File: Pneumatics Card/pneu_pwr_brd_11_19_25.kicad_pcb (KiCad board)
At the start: 4 copper layers, 65 x 65 mm, 79 parts, among them J1 2X1, J10 Conn_01x02, J11 Conn_01x02, J12 2X1, J13 2X1, J2 2X1, J3 2X1, J4 2X1, J5 2X1, J6 2X1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

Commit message: Change the M3 hole
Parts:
- C1: value 10nF -> 22nF
- C12: value 4.7u -> 0.47u
- H1, H2, H3, H4: footprint MountingHole:MountingHole_4.3mm_M4_ISO7380_Pad_TopBottom -> MountingHole:MountingHole_3.2mm_M3_DIN965
- R1: value 100k -> 1k
- R2: value 150k -> 4.7k
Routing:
- net 12V: vias 16 -> 20
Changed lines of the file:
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@@
 			)
 		)
-		(property "Value" "10nF"
+		(property "Value" "22nF"
 			(at 0 1.16 90)
 			(layer "F.Fab")
@@
 		)
 	)
-	(footprint "MountingHole:MountingHole_4.3mm_M4_ISO7380_Pad_TopBottom"
+	(footprint "MountingHole:MountingHole_3.2mm_M3_DIN965"
 		(layer "F.Cu")
 		(at 137.16 23.06)
-		(descr "Mounting Hole 4.3mm, M4, ISO7380")
-		(tags "mounting hole 4.3mm m4 iso7380")
+		(descr "Mounting Hole 3.2mm, no annular, M3, DIN965")
+		(tags "mounting hole 3.2mm no annular m3 din965")
 		(property "Reference" "H2"
-			(at 3.91 -3.34 0)
+			(at 0 -3.8 0)
 			(layer "F.SilkS")
 			(effects
@@
 		)
 		(property "Value" "MountingHole"
-			(at 0 4.8 0)
+			(at 0 3.8 0)
 			(layer "F.Fab")
 			(effects
@@
 		(fp_circle
 			(center 0 0)
-			(end 3.8 0)
+			(end 2.8 0)
 			(stroke
 				(width 0.15)
@@
 		(fp_circle
 			(center 0 0)
-			(end 4.05 0)
+			(end 3.05 0)
 			(stroke
 				(width 0.05)
@@
 			)
 		)
-		(pad "1" thru_hole circle
+		(pad "" np_thru_hole circle
 			(at 0 0)
-			(size 4.7 4.7)
-			(drill 4.3)
+			(size 3.2 3.2)
+			(drill 3.2)
 			(layers "*.Cu" "*.Mask")
-			(remove_unused_layers no)
-		)
-		(pad "1" connect circle
-			(at 0 0)
-			(size 7.6 7.6)
-			(layers "F.Cu" "F.Mask")
-		)
-		(pad "1" connect circle
-			(at 0 0)
-			(size 7.6 7.6)
-			(layers "B.Cu" "B.Mask")
 		)
 		(embedded_fonts no)
@@
 		)
 	)
-	(footprint "MountingHole:MountingHole_4.3mm_M4_ISO7380_Pad_TopBottom"
+	(footprint "MountingHole:MountingHole_3.2mm_M3_DIN965"
 		(layer "F.Cu")
 		(at 137.16 78.04)
-		(descr "Mounting Hole 4.3mm, M4, ISO7380")
-		(tags "mounting hole 4.3mm m4 iso7380")
+		(descr "Mounting Hole 3.2mm, no annular, M3, DIN965")
+		(tags "mounting hole 3.2mm no annular m3 din965")
 		(property "Reference" "H4"
-			(at 1.36 -4.72 0)
+			(at 0 -3.8 0)
 			(layer "F.SilkS")
 			(effects
@@
 		)
 		(property "Value" "MountingHole"
-			(at 0 4.8 0)
+			(at 0 3.8 0)
 			(layer "F.Fab")
 			(effects
@@
 		(fp_circle
 			(center 0 0)
-			(end 3.8 0)
+			(end 2.8 0)
 			(stroke
 				(width 0.15)
@@
 		(fp_circle
 			(center 0 0)
-			(end 4.05 0)
+			(end 3.05 0)
 			(stroke
 				(width 0.05)
@@
 			)
 		)
-		(pad "1" thru_hole circle
+		(pad "" np_thru_hole circle
 			(at 0 0)
-			(size 4.7 4.7)
-			(drill 4.3)
+			(size 3.2 3.2)
+			(drill 3.2)
 			(layers "*.Cu" "*.Mask")
-			(remove_unused_layers no)
-		)
-		(pad "1" connect circle
-			(at 0 0)
-			(size 7.6 7.6)
-			(layers "F.Cu" "F.Mask")
-		)
-		(pad "1" connect circle
-			(at 0 0)
-			(size 7.6 7.6)
-			(layers "B.Cu" "B.Mask")
 		)
 		(embedded_fonts no)
@@
 		)
 	)
-	(footprint "MountingHole:MountingHole_4.3mm_M4_ISO7380_Pad_TopBottom"
+	(footprint "MountingHole:MountingHole_3.2mm_M3_DIN965"
 		(layer "F.Cu")
 		(at 84.14 23.06)
-		(descr "Mounting Hole 4.3mm, M4, ISO7380")
-		(tags "mounting hole 4.3mm m4 iso7380")
+		(descr "Mounting Hole 3.2mm, no annular, M3, DIN965")
+		(tags "mounting hole 3.2mm no annular m3 din965")
 		(property "Reference" "H1"
-			(at 5.02 -2.67 0)
+			(at 0 -3.8 0)
 			(layer "F.SilkS")
 			(effects
@@
 		)
 		(property "Value" "MountingHole"
-			(at 0 4.8 0)
+			(at 0 3.8 0)
 			(layer "F.Fab")
 			(effects
@@
 		(fp_circle
 			(center 0 0)
-			(end 3.8 0)
+			(end 2.8 0)
 			(stroke
 				(width 0.15)
@@
 		(fp_circle
 			(center 0 0)
-			(end 4.05 0)
+			(end 3.05 0)
 			(stroke
 				(width 0.05)
@@
 			)
 		)
-		(pad "1" thru_hole circle
+		(pad "" np_thru_hole circle
 			(at 0 0)
-			(size 4.7 4.7)
-			(drill 4.3)
+			(size 3.2 3.2)
+			(drill 3.2)
 			(layers "*.Cu" "*.Mask")
-			(remove_unused_layers no)
-		)
-		(pad "1" connect circle
-			(at 0 0)
-			(size 7.6 7.6)
-			(layers "F.Cu" "F.Mask")
-		)
-		(pad "1" connect circle
-			(at 0 0)
-			(size 7.6 7.6)
-			(layers "B.Cu" "B.Mask")
 		)
 		(embedded_fonts no)
@@
 			)
 		)
-		(property "Value" "150k"
+		(property "Value" "4.7k"
 			(at 0 1.17 90)
 			(layer "F.Fab")
@@
 		)
 	)
-	(footprint "MountingHole:MountingHole_4.3mm_M4_ISO7380_Pad_TopBottom"
+	(footprint "MountingHole:MountingHole_3.2mm_M3_DIN965"
 		(layer "F.Cu")
 		(at 84.14 78.04)
-		(descr "Mounting Hole 4.3mm, M4, ISO7380")
-		(tags "mounting hole 4.3mm m4 iso7380")
+		(descr "Mounting Hole 3.2mm, no annular, M3, DIN965")
+		(tags "mounting hole 3.2mm no annular m3 din965")
 		(property "Reference" "H3"
-			(at 0 -4.8 0)
+			(at 0 -3.8 0)
 			(layer "F.SilkS")
 			(effects
@@
 		)
 		(property "Value" "MountingHole"
-			(at 0 4.8 0)
+			(at 0 3.8 0)
 			(layer "F.Fab")
 			(effects
@@
 		(fp_circle
 			(center 0 0)
-			(end 3.8 0)
+			(end 2.8 0)
 			(stroke
 				(width 0.15)
@@
 		(fp_circle
 			(center 0 0)
-			(end 4.05 0)
+			(end 3.05 0)
 			(stroke
 				(width 0.05)
@@
 			)
 		)
-		(pad "1" thru_hole circle
+		(pad "" np_thru_hole circle
 			(at 0 0)
-			(size 4.7 4.7)
-			(drill 4.3)
+			(size 3.2 3.2)
+			(drill 3.2)
 			(layers "*.Cu" "*.Mask")
-			(remove_unused_layers no)
-		)
-		(pad "1" connect circle
-			(at 0 0)
-			(size 7.6 7.6)
-			(layers "F.Cu" "F.Mask")
-		)
-		(pad "1" connect circle
-			(at 0 0)
-			(size 7.6 7.6)
-			(layers "B.Cu" "B.Mask")
 		)
 		(embedded_fonts no)
@@
 			)
 		)
-		(property "Value" "100k"
+		(property "Value" "1k"
 			(at 0 1.17 90)
 			(layer "F.Fab")
@@
 			)
 		)
-		(property "Value" "4.7u"
+		(property "Value" "0.47u"
 			(at 0 1.16 90)
 			(layer "F.Fab")
@@
 	)
 	(via
+		(at 89.58 70.41)
+		(size 0.8)
+		(drill 0.4)
+		(layers "F.Cu" "B.Cu")
+		(free yes)
+		(net 13)
+	)
+	(via
 		(at 92.59 71.38)
 		(size 0.8)
@@
 	)
 	(via
+		(at 91.58 70.41)
+		(size 0.8)
+		(drill 0.4)
+		(layers "F.Cu" "B.Cu")
+		(free yes)
+		(net 13)
+	)
+	(via
 		(at 90.6 73.36)
 		(size 0.8)
@@
 	)
 	(via
+		(at 90.58 70.41)
+		(size 0.8)
+		(drill 0.4)
+		(layers "F.Cu" "B.Cu")
+		(free yes)
+		(net 13)
+	)
+	(via
 		(at 89.4025 42.6925)
 		(size 0.8)
@@
 		(size 0.8)
 		(drill 0.4)
+		(layers "F.Cu" "B.Cu")
+		(free yes)
+		(net 13)
+	)
+	(via
+		(at 92.57 70.43)
+		(size 0.8)
+		(drill 0.4)

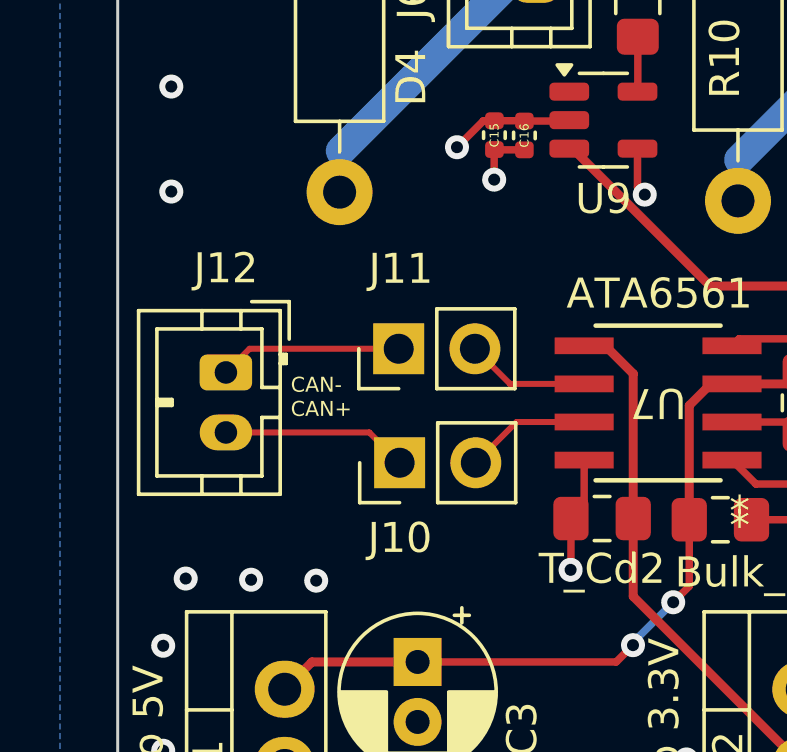
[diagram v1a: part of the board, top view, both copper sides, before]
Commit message: Corrected CANBUS routing Length.
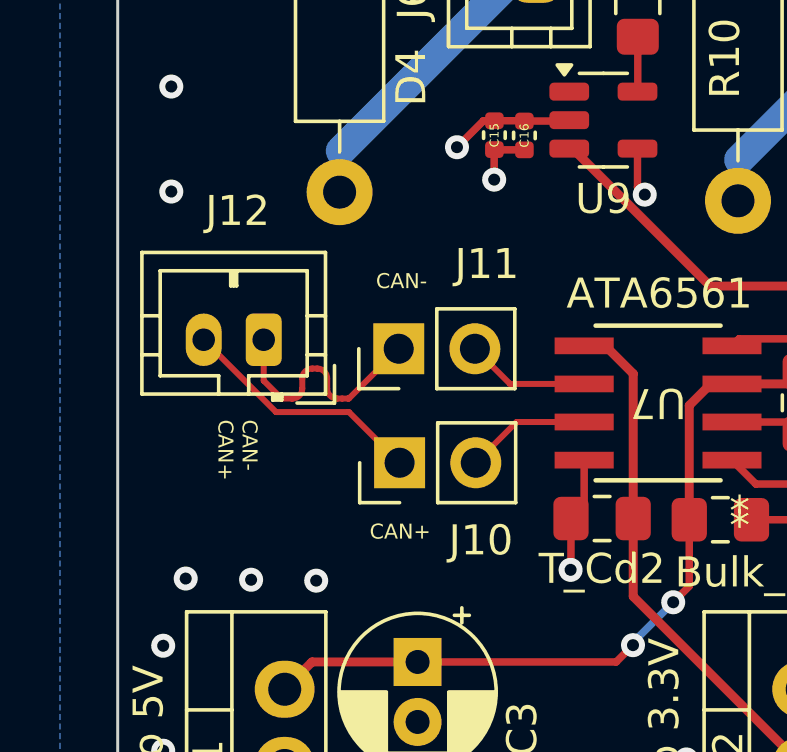
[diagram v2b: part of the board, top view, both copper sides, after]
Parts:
- moved J12 1.67 mm to (83.0, 49.1), turned to 180 degrees
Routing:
- net CAN-: track 10.2 -> 12.3 mm
- net CAN+: track 10.4 -> 12.4 mm
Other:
- board text added: "CAN+"
- board text added: "CAN-"

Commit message: Changed resistor values
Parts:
- C1: value 22nF -> 2.2uF
- R1: value 1k -> 47k
- R2: value 4.7k -> 10k
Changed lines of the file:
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@@
 			(psa4output no)
 			(plot_black_and_white yes)
-			(plotinvisibletext no)
 			(sketchpadsonfab no)
 			(plotpadnumbers no)
@@
 			)
 		)
-		(property "Datasheet" ""
+		(property "Datasheet" "~"
 			(at 0 0 90)
 			(unlocked yes)
@@
 			)
 		)
-		(property "Datasheet" ""
+		(property "Datasheet" "~"
 			(at 0 0 180)
 			(unlocked yes)
@@
 			)
 		)
-		(property "Datasheet" ""
+		(property "Datasheet" "~"
 			(at 0 0 90)
 			(unlocked yes)
@@
 			)
 		)
-		(property "Datasheet" ""
+		(property "Datasheet" "~"
 			(at 0 0 90)
 			(unlocked yes)
@@
 			)
 		)
-		(property "Datasheet" ""
+		(property "Datasheet" "~"
 			(at 0 0 90)
 			(layer "F.Fab")
@@
 			)
 		)
-		(property "Datasheet" ""
+		(property "Datasheet" "~"
 			(at 0 0 90)
 			(unlocked yes)
@@
 			)
 		)
-		(property "Datasheet" ""
+		(property "Datasheet" "~"
 			(at 0 0 90)
 			(layer "F.Fab")
@@
 			)
 		)
-		(property "Datasheet" ""
+		(property "Datasheet" "~"
 			(at 0 0 90)
 			(unlocked yes)
@@
 			)
 		)
-		(property "Value" "22nF"
+		(property "Value" "2.2uF"
 			(at 0 1.16 90)
 			(layer "F.Fab")
@@
 			)
 		)
-		(property "Datasheet" ""
+		(property "Datasheet" "~"
 			(at 0 0 90)
 			(unlocked yes)
@@
 			)
 		)
-		(property "Datasheet" ""
+		(property "Datasheet" "~"
 			(at 0 0 0)
 			(unlocked yes)
@@
 			)
 		)
-		(property "Datasheet" ""
+		(property "Datasheet" "~"
 			(at 0 0 0)
 			(unlocked yes)
@@
 			)
 		)
-		(property "Datasheet" ""
+		(property "Datasheet" "~"
 			(at 0 0 0)
 			(unlocked yes)
@@
 			)
 		)
-		(property "Datasheet" ""
+		(property "Datasheet" "~"
 			(at 0 0 90)
 			(layer "F.Fab")
@@
 			)
 		)
-		(property "Datasheet" ""
+		(property "Datasheet" "~"
 			(at 0 0 180)
 			(unlocked yes)
@@
 			)
 		)
-		(property "Datasheet" ""
+		(property "Datasheet" "~"
 			(at 0 0 0)
 			(layer "F.Fab")
@@
 			)
 		)
-		(property "Datasheet" ""
+		(property "Datasheet" "~"
 			(at 0 0 0)
 			(unlocked yes)
@@
 			)
 		)
-		(property "Datasheet" ""
+		(property "Datasheet" "~"
 			(at 0 0 0)
 			(unlocked yes)
@@
 			)
 		)
-		(property "Datasheet" ""
+		(property "Datasheet" "~"
 			(at 0 0 0)
 			(unlocked yes)
@@
 			)
 		)
-		(property "Datasheet" ""
+		(property "Datasheet" "~"
 			(at 0 0 0)
 			(unlocked yes)
@@
 			)
 		)
-		(property "Datasheet" ""
+		(property "Datasheet" "~"
 			(at 0 0 270)
 			(unlocked yes)
@@
 			)
 		)
-		(property "Datasheet" ""
+		(property "Datasheet" "~"
 			(at 0 0 0)
 			(unlocked yes)
@@
 			)
 		)
-		(property "Datasheet" ""
+		(property "Datasheet" "~"
 			(at 0 0 0)
 			(unlocked yes)
@@
 			)
 		)
-		(property "Datasheet" ""
+		(property "Datasheet" "~"
 			(at 0 0 90)
 			(unlocked yes)
@@
 			)
 		)
-		(property "Datasheet" ""
+		(property "Datasheet" "~"
 			(at 0 0 0)
 			(unlocked yes)
@@
 			)
 		)
-		(property "Datasheet" ""
+		(property "Datasheet" "~"
 			(at 0 0 0)
 			(layer "F.Fab")
@@
 			)
 		)
-		(property "Datasheet" ""
+		(property "Datasheet" "~"
 			(at 0 0 270)
 			(unlocked yes)
@@
 			)
 		)
-		(property "Datasheet" ""
+		(property "Datasheet" "~"
 			(at 0 0 270)
 			(unlocked yes)
@@
 			)
 		)
-		(property "Datasheet" ""
+		(property "Datasheet" "~"
 			(at 0 0 270)
 			(unlocked yes)
@@
 			)
 		)
-		(property "Datasheet" ""
+		(property "Datasheet" "~"
 			(at 0 0 180)
 			(unlocked yes)
@@
 			)
 		)
-		(property "Datasheet" ""
+		(property "Datasheet" "~"
 			(at 0 0 90)
 			(layer "F.Fab")
@@
 			)
 		)
-		(property "Datasheet" ""
+		(property "Datasheet" "~"
 			(at 0 0 90)
 			(unlocked yes)
@@
 			)
 		)
-		(property "Datasheet" ""
+		(property "Datasheet" "~"
 			(at 0 0 180)
 			(unlocked yes)
@@
 			)
 		)
-		(property "Value" "4.7k"
+		(property "Value" "10k"
 			(at 0 1.17 90)
 			(layer "F.Fab")
@@
 			)
 		)
-		(property "Datasheet" ""
+		(property "Datasheet" "~"
 			(at 0 0 90)
 			(layer "F.Fab")
@@
 			)
 		)
-		(property "Datasheet" ""
+		(property "Datasheet" "~"
 			(at 0 0 180)
 			(unlocked yes)
@@
 			)
 		)
-		(property "Datasheet" ""
+		(property "Datasheet" "~"
 			(at 0 0 90)
 			(unlocked yes)
@@
 			)
 		)
-		(property "Datasheet" ""
+		(property "Datasheet" "~"
 			(at 0 0 270)
 			(unlocked yes)
@@
 			)
 		)
-		(property "Datasheet" ""
+		(property "Datasheet" "~"
 			(at 0 0 90)
 			(layer "F.Fab")
@@
 			)
 		)
-		(property "Datasheet" ""
+		(property "Datasheet" "~"
 			(at 0 0 0)
 			(unlocked yes)
@@
 			)
 		)
-		(property "Value" "1k"
+		(property "Value" "47k"
 			(at 0 1.17 90)
 			(layer "F.Fab")
@@
 			)
 		)
-		(property "Datasheet" ""
+		(property "Datasheet" "~"
 			(at 0 0 90)
 			(layer "F.Fab")
@@
 			)
 		)
-		(property "Datasheet" ""
+		(property "Datasheet" "~"
 			(at 0 0 90)
 			(unlocked yes)
@@
 			)
 		)
-		(property "Datasheet" ""
+		(property "Datasheet" "~"
 			(at 0 0 90)
 			(unlocked yes)
@@
 			)
 		)
-		(property "Datasheet" ""
+		(property "Datasheet" "~"
 			(at 0 0 0)
 			(layer "F.Fab")
@@
 			)
 		)
-		(property "Datasheet" ""
+		(property "Datasheet" "~"
 			(at 0 0 90)
 			(unlocked yes)
@@
 			)
 		)
-		(property "Datasheet" ""
+		(property "Datasheet" "~"
 			(at 0 0 90)
 			(unlocked yes)

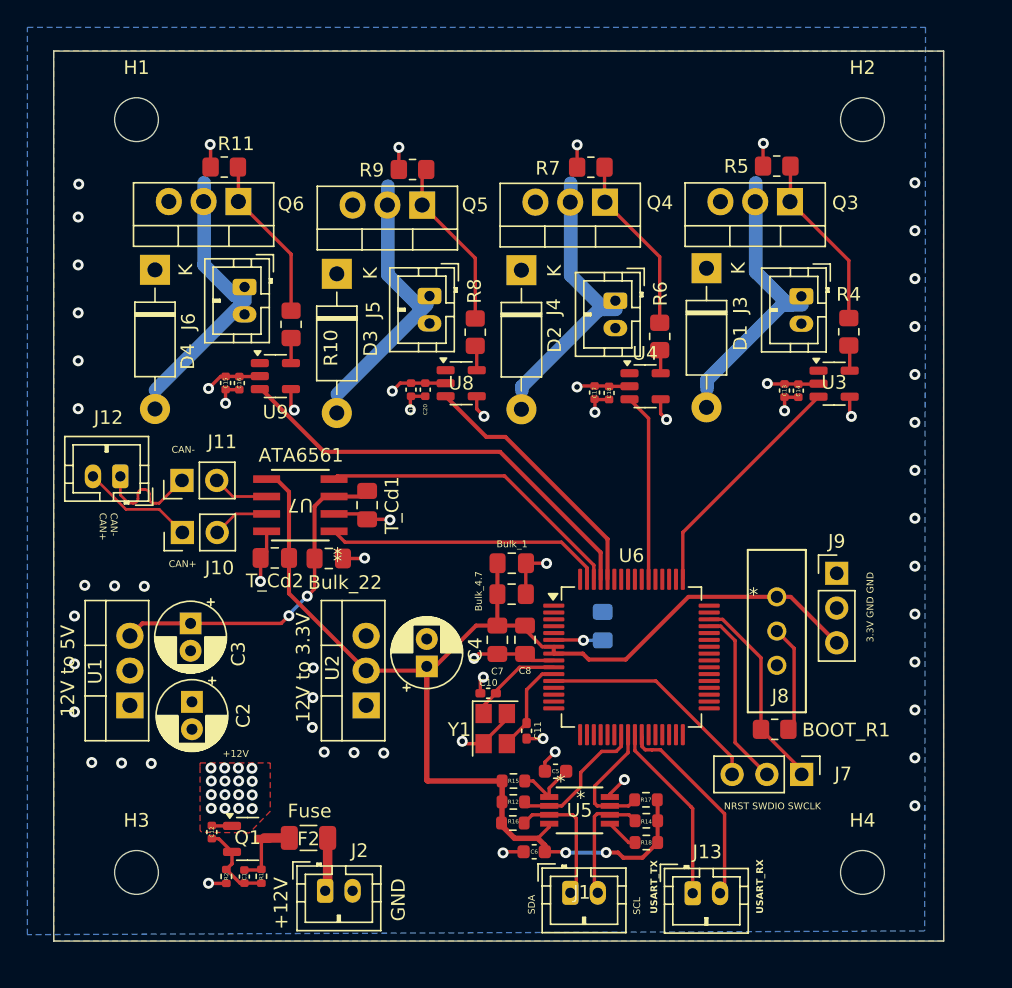
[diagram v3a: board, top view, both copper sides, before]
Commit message: fixed the traces, added test point, fixed some silkscreen
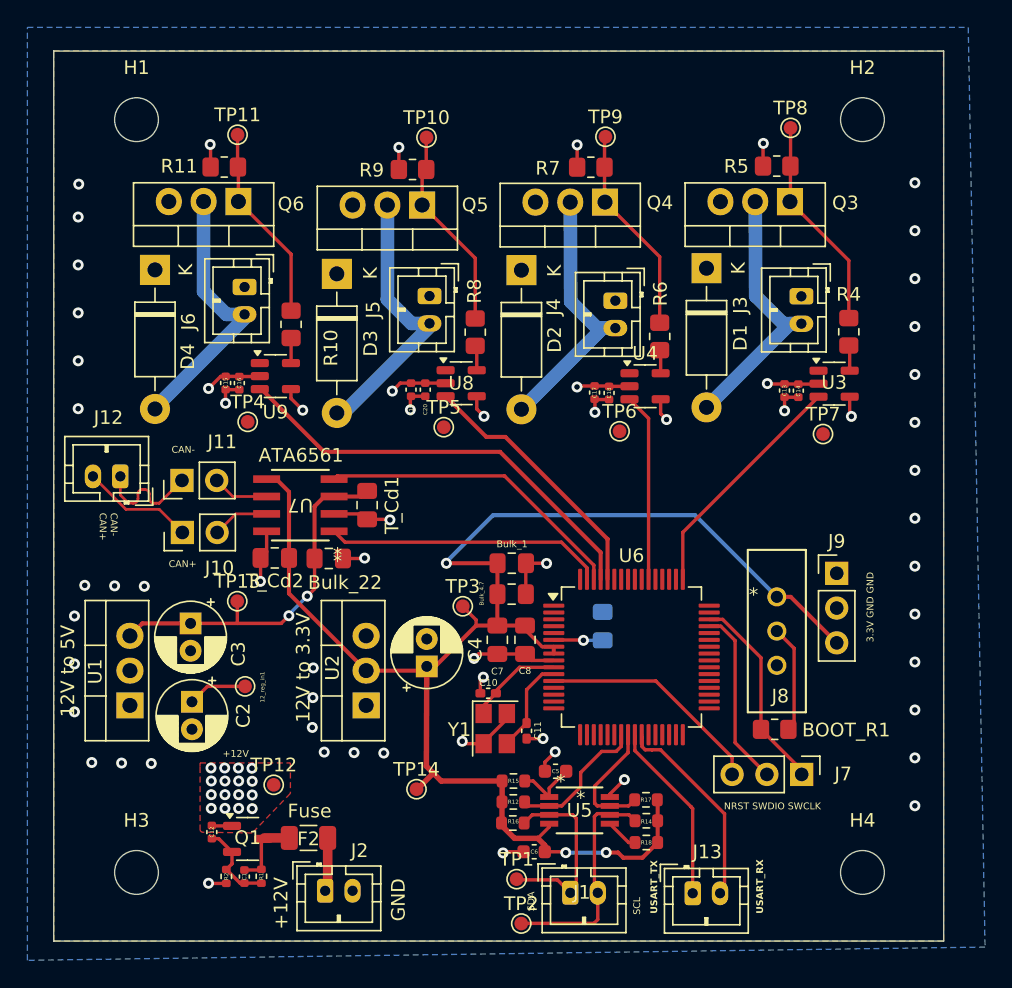
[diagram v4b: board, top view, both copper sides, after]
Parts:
- added 12_reg_in1: 12_reg_in, TestPoint:TestPoint_Pad_D1.0mm, F.Cu at (92.1, 64.5)
- added TP1: SDA_ext, TestPoint:TestPoint_Pad_D1.0mm, F.Cu at (111.9, 78.5)
- added TP10: S3_out, TestPoint:TestPoint_Pad_D1.0mm, F.Cu at (105.3, 24.4)
- added TP11: S4_out, TestPoint:TestPoint_Pad_D1.0mm, F.Cu at (91.5, 24.2)
- added TP12: 12V_PWR, TestPoint:TestPoint_Pad_D1.0mm, F.Cu at (94.2, 71.6)
- added TP13: 5_reg_out, TestPoint:TestPoint_Pad_D1.0mm, F.Cu at (91.5, 58.2)
- added TP14: 3.3_reg_out, TestPoint:TestPoint_Pad_D1.0mm, F.Cu at (104.6, 72.0)
- added TP2: SCL_ext, TestPoint:TestPoint_Pad_D1.0mm, F.Cu at (112.2, 81.8)
- added TP3: STM_PWR, TestPoint:TestPoint_Pad_D1.0mm, F.Cu at (108.0, 58.6)
- added TP4: S4_in, TestPoint:TestPoint_Pad_D1.0mm, F.Cu at (92.3, 45.1)
- added TP5: S3_in, TestPoint:TestPoint_Pad_D1.0mm, F.Cu at (106.6, 45.5)
- added TP6: S2_in, TestPoint:TestPoint_Pad_D1.0mm, F.Cu at (119.4, 45.8)
- added TP7: S1_in, TestPoint:TestPoint_Pad_D1.0mm, F.Cu at (134.3, 46.0)
- added TP8: S1_out, TestPoint:TestPoint_Pad_D1.0mm, F.Cu at (131.9, 23.7)
- added TP9: S2_out, TestPoint:TestPoint_Pad_D1.0mm, F.Cu at (118.4, 24.3)
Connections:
- J13 pad 1: USART- -> USART1_TX
- J13 pad 2: USART+ -> USART1_RX
- U6 pad 19: USART1+ -> unconnected-(U6-PA2-Pad19)
- U6 pad 20: USART1- -> unconnected-(U6-PA3-Pad20)
- U6 pad 25: unconnected-(U6-PC4-Pad25) -> USART1_TX
- U6 pad 26: unconnected-(U6-PC5-Pad26) -> USART1_RX
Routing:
- net 12V: track 17.4 -> 75.9 mm, vias 20 -> 79
- net GND: track 54.1 -> 0.00 mm, vias 59 -> 0
- net (no net): track 28.2 -> 0.00 mm
- net 3.3V: track 97.4 -> 114.0 mm, vias 2 -> 3
- net USART1_RX: track 0.00 -> 14.9 mm
- net USART1_TX: track 0.00 -> 13.3 mm
- net SCL_ext: track 8.28 -> 16.0 mm
- net SDA_ext: track 9.72 -> 13.9 mm
- net Net-(Q3-G): track 12.9 -> 15.7 mm
- net Net-(Q6-G): track 12.1 -> 14.6 mm
- net Net-(Q4-G): track 13.0 -> 15.4 mm
- net Net-(Q5-G): track 12.6 -> 14.8 mm
- net 5V: track 25.3 -> 26.9 mm
- added copper zone on B.Cu, net 12V
- added copper zone on In1.Cu, net 12V
- removed copper zone on B.Cu, net GND
- removed copper zone on F.Cu, net GND
- removed copper zone on In1.Cu, net GND
